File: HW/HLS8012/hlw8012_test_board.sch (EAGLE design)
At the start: 36 parts, among them T2 2N3904, T3 2N3904, T4 2N3904

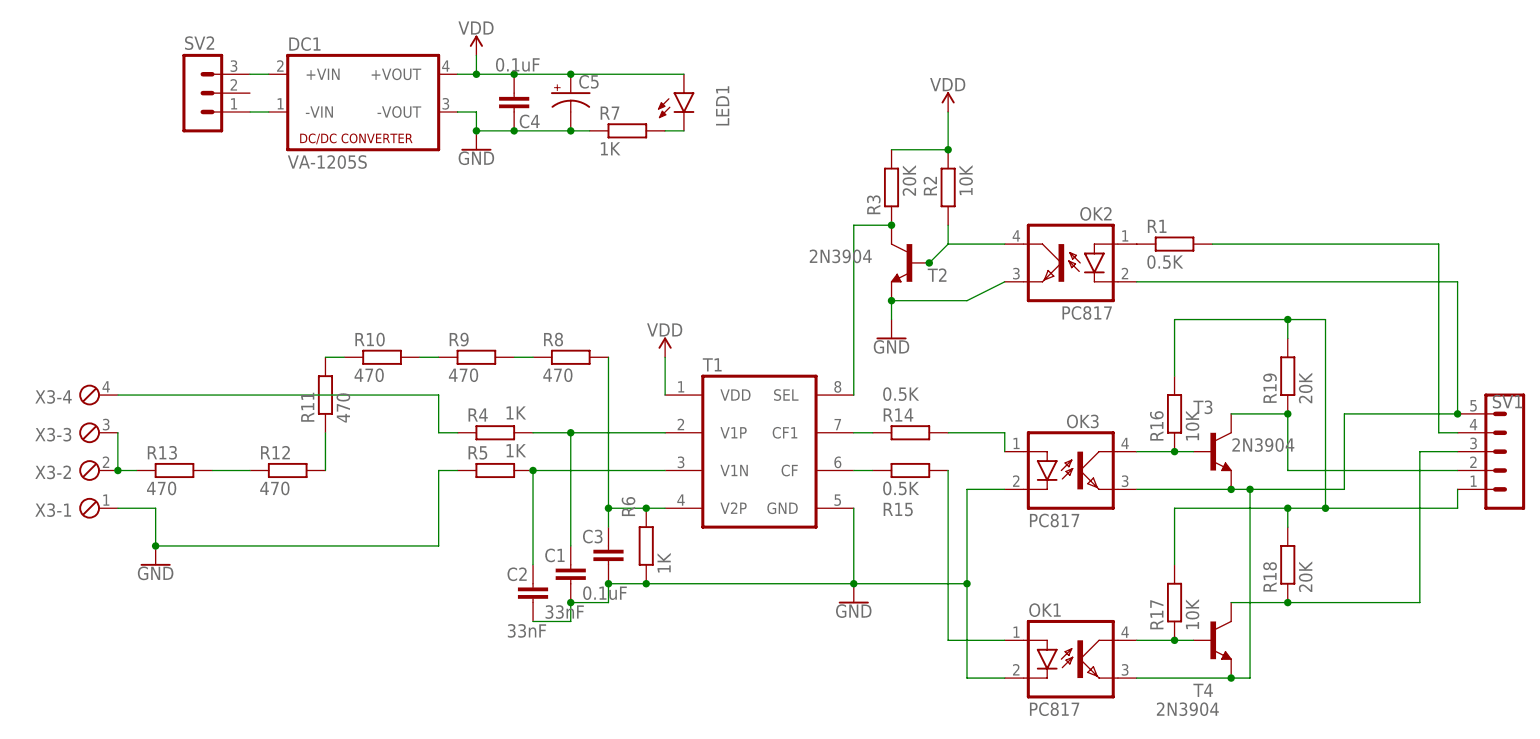
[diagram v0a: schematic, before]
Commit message: Refactored hlw board
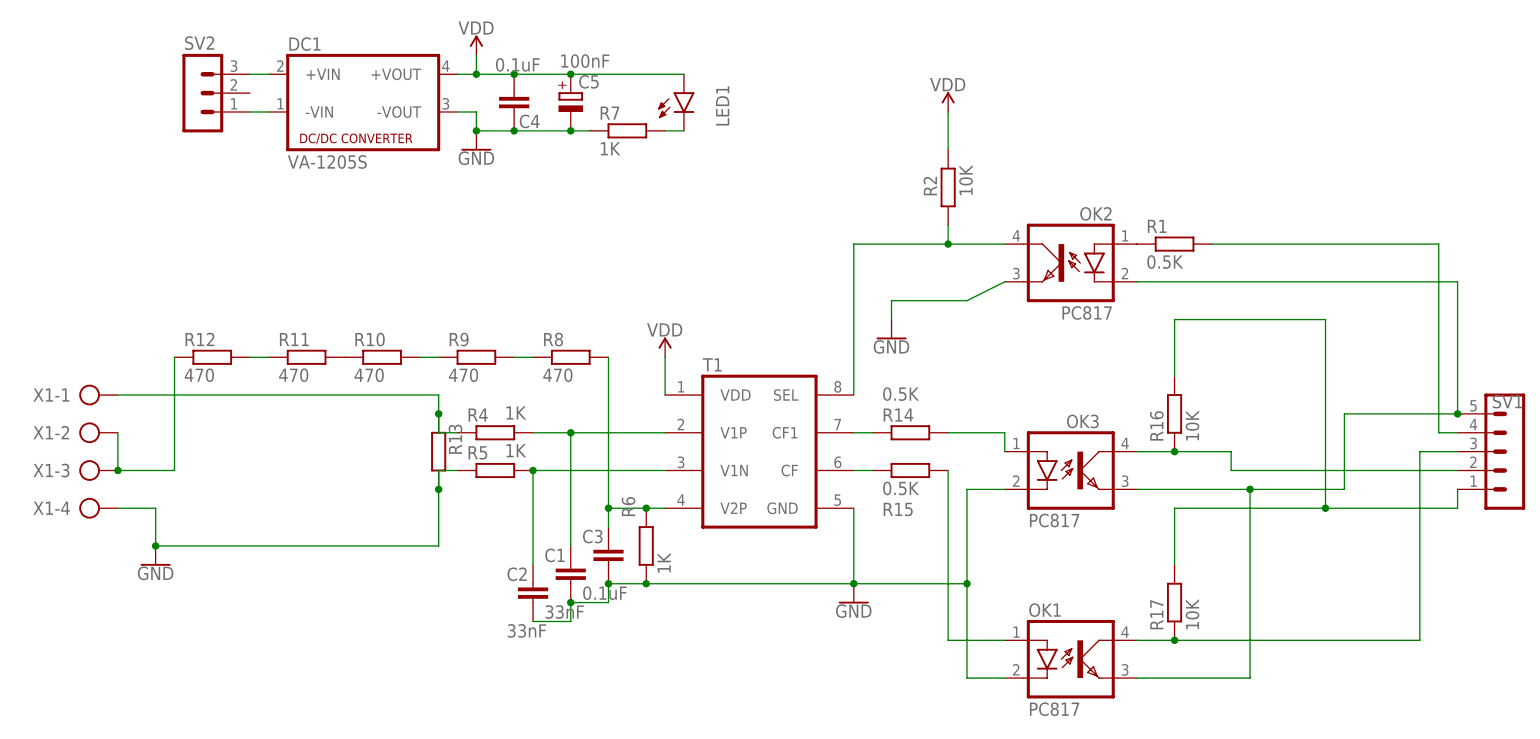
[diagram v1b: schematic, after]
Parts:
- removed R18, R19, R3: 20K, rcl:R-EU_M0805
- removed T2, T3, T4: 2N3904, transistor:2N3904
- removed X3: (no value), con-phoenix-254:MPT4
- added X1: (no value), con-ptr500:AK300/4
- C5: value (none) -> 100nF; device antduino:SPARKFUN_CAP_POLPTH1 -> rcl:CPOL-EU153CLV-0810
- R13: value 470 -> (none); device rcl:R-EU_M0805 -> resistor-shunt:PMD
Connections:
- removed net N$11: OK1.COL, R17.1, T4.B
- removed net N$13: R19.1, SV1.2, T3.C
- removed net N$29: R12.1, R13.2
- removed net N$5: R3.1, T1.SEL, T2.C
- net GND: now also R13.1, X1-4.KL; no longer T2.E, X3-1.1
- net N$1: no longer R18.2, R19.2
- net N$12: now also OK1.COL, R17.1; no longer R18.1, T4.C
- net N$16: no longer T3.E, T4.E
- net N$17: now also R13.2, X1-1.KL; no longer X3-4.1
- net N$30: now also R12.1, X1-2.KL, X1-3.KL; no longer R13.1, X3-2.1, X3-3.1
- net N$4: now also T1.SEL; no longer T2.B
- net N$6: now also SV1.2; no longer T3.B
- net VDD: no longer R3.2
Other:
- moved on the sheet: R11, R12, R13

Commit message: Updated hlw board. Added libs
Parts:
- removed OK1: PC817, optocoupler:PC817
- removed R15: 0.5K, rcl:R-EU_M0805
- removed R17: 10K, rcl:R-EU_M0805
- C5: value 100nF -> 10uF; device rcl:CPOL-EU153CLV-0810 -> rcl:CPOL-EU153CLV-0405
- DC1: value VA-1205S -> VA-0505S1; device dc-dc-converter:VA-1205S -> dc-dc-converter:VA-0505S1
- R16: value 10K -> 2K
- R2: value 10K -> 5K
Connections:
- removed net N$10: R15.1, T1.CF
- removed net N$12: OK1.COL, R17.1, SV1.3
- removed net N$8: OK3.A, R14.2
- net GND: no longer OK1.C, OK3.C
- net N$1: now also OK2.A; no longer R17.2
- net N$16: no longer OK1.EMIT, OK2.C
- net N$2: now also OK2.C, R1.1; no longer R1.2, SV1.4
- net N$3: now also R1.2, SV1.2; no longer OK2.A, R1.1
- net N$6: now also SV1.4; no longer SV1.2
- net N$7: now also OK3.C, R14.2; no longer OK1.A, R15.2
- net VDD: now also OK3.A
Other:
- moved on the sheet: OK3, R1, R14, R16
